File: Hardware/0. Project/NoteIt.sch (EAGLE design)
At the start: 65 parts, among them CN1 USB 3.2 Gen 2 Type C Receptac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, CN2 Lithium Ion Polymer, CN3 OSTTE020104, CN4 FTSH-105-01-L-DV-K-TR, CN5 CR1220, CN6 Micro-SD Card, Q1 BC817, Q2 SI2374DS, Q3 SI2374DS, SW1 KY-040, U1 MCP73831/2, U2 MSP430FR2476TPTR, U3 S-8261ACMMD-G4MT2U, U4 GL823K, U5 SN74AHC1G125DBV, U6 TS3A27518EPWR, U7 TLV75530PDBVR, U8 DS3231/SO, Y1 32.768 kHz

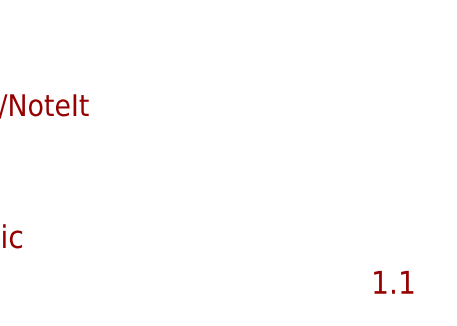
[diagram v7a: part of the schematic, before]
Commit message: NoteIt v1.2 release (details in commit description)
- All vias changed to 0.3mm drill with 0.6mm diameter.
- This approach saves money in the production of PCBs (JLCPCB experience) - less tests is necessary.
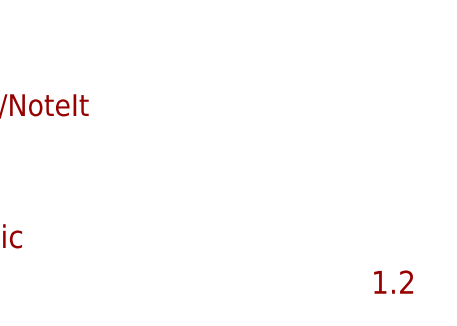
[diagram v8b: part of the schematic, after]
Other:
- note added: "1.2"
- note removed: "1.1"
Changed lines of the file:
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@@
 <text x="487.172" y="28.067" size="3.81" layer="94" align="center">Tiago Silva</text>
 <text x="487.172" y="22.225" size="2.413" layer="94" align="center">github.com/TiagoPaulaSilva/NoteIt</text>
-<text x="544.195" y="1.27" size="2.54" layer="94" ratio="5">1.1</text>
+<text x="544.195" y="1.27" size="2.54" layer="94" ratio="5">1.2</text>
 <text x="473.075" y="6.35" size="2.54" layer="94" ratio="5">Complete Schematic</text>
 <text x="437.515" y="183.515" size="1.27" layer="98" align="center" grouprefs="ROTARY_ENCODER">needs MCU pull-up</text>
@@
 <wire x1="180.34" y1="373.38" x2="179.07" y2="374.015" width="0.1524" layer="208" grouprefs="POWER_SUPPLY BATTERY_PROTECTOR"/>
 <text x="182.499" y="375.793" size="1.27" layer="208" align="center" grouprefs="POWER_SUPPLY BATTERY_PROTECTOR">7μA max.</text>
-<text x="75.565" y="334.01" size="1.27" layer="208" font="vector" align="center" grouprefs="BATTERY_CHARGING_MANAGER POWER_SUPPLY">I-REG [mA]
+<text x="75.565" y="334.01" size="1.27" layer="208" font="vector" align="center" grouprefs="POWER_SUPPLY BATTERY_CHARGING_MANAGER">I-REG [mA]
 = 1000V / R-PROG</text>
-<wire x1="100.965" y1="379.73" x2="107.315" y2="379.73" width="0.1524" layer="208" grouprefs="BATTERY_CHARGING_MANAGER POWER_SUPPLY"/>
-<wire x1="107.315" y1="379.73" x2="106.045" y2="379.095" width="0.1524" layer="208" grouprefs="BATTERY_CHARGING_MANAGER POWER_SUPPLY"/>
-<wire x1="106.045" y1="379.095" x2="106.045" y2="380.365" width="0.1524" layer="208" grouprefs="BATTERY_CHARGING_MANAGER POWER_SUPPLY"/>
-<wire x1="106.045" y1="380.365" x2="107.315" y2="379.73" width="0.1524" layer="208" grouprefs="BATTERY_CHARGING_MANAGER POWER_SUPPLY"/>
-<text x="105.156" y="376.682" size="1.27" layer="208" rot="R180" align="center" grouprefs="BATTERY_CHARGING_MANAGER POWER_SUPPLY">15mA to
+<wire x1="100.965" y1="379.73" x2="107.315" y2="379.73" width="0.1524" layer="208" grouprefs="POWER_SUPPLY BATTERY_CHARGING_MANAGER"/>
+<wire x1="107.315" y1="379.73" x2="106.045" y2="379.095" width="0.1524" layer="208" grouprefs="POWER_SUPPLY BATTERY_CHARGING_MANAGER"/>
+<wire x1="106.045" y1="379.095" x2="106.045" y2="380.365" width="0.1524" layer="208" grouprefs="POWER_SUPPLY BATTERY_CHARGING_MANAGER"/>
+<wire x1="106.045" y1="380.365" x2="107.315" y2="379.73" width="0.1524" layer="208" grouprefs="POWER_SUPPLY BATTERY_CHARGING_MANAGER"/>
+<text x="105.156" y="376.682" size="1.27" layer="208" rot="R180" align="center" grouprefs="POWER_SUPPLY BATTERY_CHARGING_MANAGER">15mA to
 500mA max.</text>
 <text x="332.105" y="393.065" size="1.778" layer="208" align="center" grouprefs="POWER_SUPPLY VOLTAGE_REGULATOR">238mV drops
@@
 <text x="262.89" y="395.605" size="0.254" layer="201" align="center" grouprefs="BATTERY_MONITOR POWER_SUPPLY"> </text>
 <text x="182.88" y="395.605" size="0.254" layer="91" align="center" grouprefs="POWER_SUPPLY BATTERY_PROTECTOR"> </text>
-<text x="44.45" y="395.605" size="0.254" layer="91" align="center" grouprefs="BATTERY_CHARGING_MANAGER POWER_SUPPLY"> </text>
+<text x="44.45" y="395.605" size="0.254" layer="91" align="center" grouprefs="POWER_SUPPLY BATTERY_CHARGING_MANAGER"> </text>
 <wire x1="249.555" y1="236.855" x2="278.765" y2="236.855" width="0.254" layer="204" style="shortdash" grouprefs="MICRO_SDCARD_CONTROLLER"/>
 <wire x1="278.765" y1="236.855" x2="278.765" y2="213.995" width="0.254" layer="204" style="shortdash" grouprefs="MICRO_SDCARD_CONTROLLER"/>
@@
 <attribute name="VALUE" x="460.756" y="189.103" size="1.27" layer="96" align="center"/>
 </instance>
-<instance part="U1" gate="G$1" x="85.09" y="376.555" smashed="yes" grouprefs="BATTERY_CHARGING_MANAGER POWER_SUPPLY">
+<instance part="U1" gate="G$1" x="85.09" y="376.555" smashed="yes" grouprefs="POWER_SUPPLY BATTERY_CHARGING_MANAGER">
 <attribute name="NAME" x="78.8035" y="387.35" size="1.27" layer="95" align="center"/>
 <attribute name="VALUE" x="82.55" y="385.445" size="1.27" layer="96" align="center"/>
 </instance>
-<instance part="R5" gate="G$1" x="62.23" y="334.01" smashed="yes" rot="R90" grouprefs="BATTERY_CHARGING_MANAGER POWER_SUPPLY">
+<instance part="R5" gate="G$1" x="62.23" y="334.01" smashed="yes" rot="R90" grouprefs="POWER_SUPPLY BATTERY_CHARGING_MANAGER">
 <attribute name="NAME" x="60.0964" y="334.01" size="1.27" layer="95" rot="R90" align="center"/>
 <attribute name="VALUE" x="64.262" y="334.01" size="1.27" layer="96" rot="R90" align="center"/>
@@
 <segment>
 <pinref part="R5" gate="G$1" pin="1"/>
-<wire x1="62.23" y1="328.93" x2="62.23" y2="313.69" width="0.1524" layer="91" grouprefs="BATTERY_CHARGING_MANAGER POWER_SUPPLY"/>
+<wire x1="62.23" y1="328.93" x2="62.23" y2="313.69" width="0.1524" layer="91" grouprefs="POWER_SUPPLY BATTERY_CHARGING_MANAGER"/>
 <pinref part="U1" gate="G$1" pin="VSS"/>
-<wire x1="88.9" y1="342.265" x2="88.9" y2="313.69" width="0.1524" layer="91" grouprefs="BATTERY_CHARGING_MANAGER POWER_SUPPLY"/>
-<wire x1="88.9" y1="313.69" x2="62.23" y2="313.69" width="0.1524" layer="91" grouprefs="BATTERY_CHARGING_MANAGER POWER_SUPPLY"/>
+<wire x1="88.9" y1="342.265" x2="88.9" y2="313.69" width="0.1524" layer="91" grouprefs="POWER_SUPPLY BATTERY_CHARGING_MANAGER"/>
+<wire x1="88.9" y1="313.69" x2="62.23" y2="313.69" width="0.1524" layer="91" grouprefs="POWER_SUPPLY BATTERY_CHARGING_MANAGER"/>
 <pinref part="R7" gate="G$1" pin="1"/>
 <wire x1="123.19" y1="313.69" x2="123.19" y2="316.23" width="0.1524" layer="91" grouprefs="POWER_SUPPLY"/>
 <junction x="123.19" y="313.69" grouprefs="POWER_SUPPLY"/>
 <wire x1="88.9" y1="313.69" x2="123.19" y2="313.69" width="0.1524" layer="91" grouprefs="POWER_SUPPLY"/>
-<junction x="88.9" y="313.69" grouprefs="BATTERY_CHARGING_MANAGER POWER_SUPPLY"/>
+<junction x="88.9" y="313.69" grouprefs="POWER_SUPPLY BATTERY_CHARGING_MANAGER"/>
 <wire x1="215.265" y1="326.39" x2="215.265" y2="313.69" width="0.1524" layer="91" grouprefs="POWER_SUPPLY"/>
 <wire x1="215.265" y1="313.69" x2="123.19" y2="313.69" width="0.1524" layer="91" grouprefs="POWER_SUPPLY"/>
@@
 <pinref part="U1" gate="G$1" pin="PROG"/>
 <pinref part="R5" gate="G$1" pin="2"/>
-<wire x1="72.39" y1="353.695" x2="62.23" y2="353.695" width="0.1524" layer="91" grouprefs="BATTERY_CHARGING_MANAGER POWER_SUPPLY"/>
-<wire x1="62.23" y1="353.695" x2="62.23" y2="339.09" width="0.1524" layer="91" grouprefs="BATTERY_CHARGING_MANAGER POWER_SUPPLY"/>
+<wire x1="72.39" y1="353.695" x2="62.23" y2="353.695" width="0.1524" layer="91" grouprefs="POWER_SUPPLY BATTERY_CHARGING_MANAGER"/>
+<wire x1="62.23" y1="353.695" x2="62.23" y2="339.09" width="0.1524" layer="91" grouprefs="POWER_SUPPLY BATTERY_CHARGING_MANAGER"/>
 </segment>
 </net>
